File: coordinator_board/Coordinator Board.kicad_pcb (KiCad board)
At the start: 2 copper layers, 42.5 x 27 mm, 19 parts, among them P1 POWER, P4 SERIAL, SW1 Switch_SPDT_x2, SW2 Switch_DPST, U1 LM3671, U3 ESP-12E, U4 DIY-OLED-0.96, U5 SF303GJ26

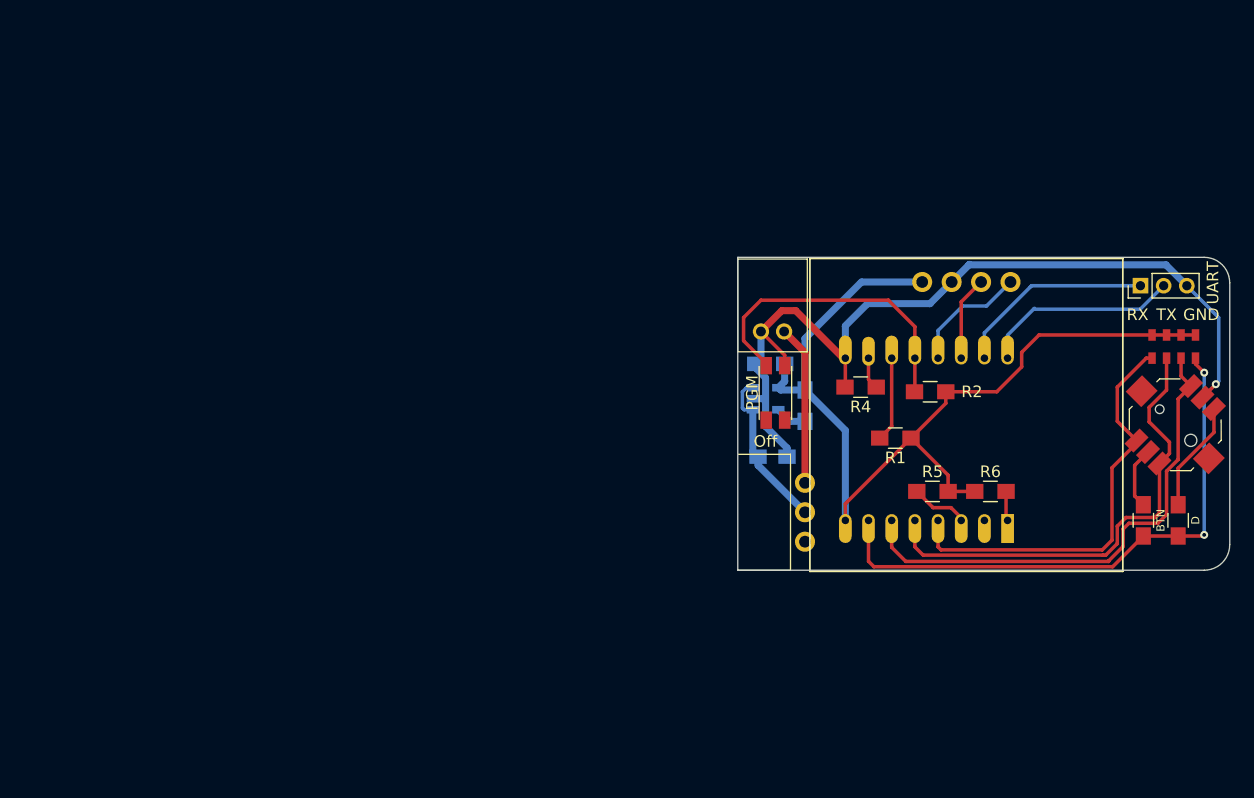
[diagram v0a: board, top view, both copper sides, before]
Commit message: Created new part layout
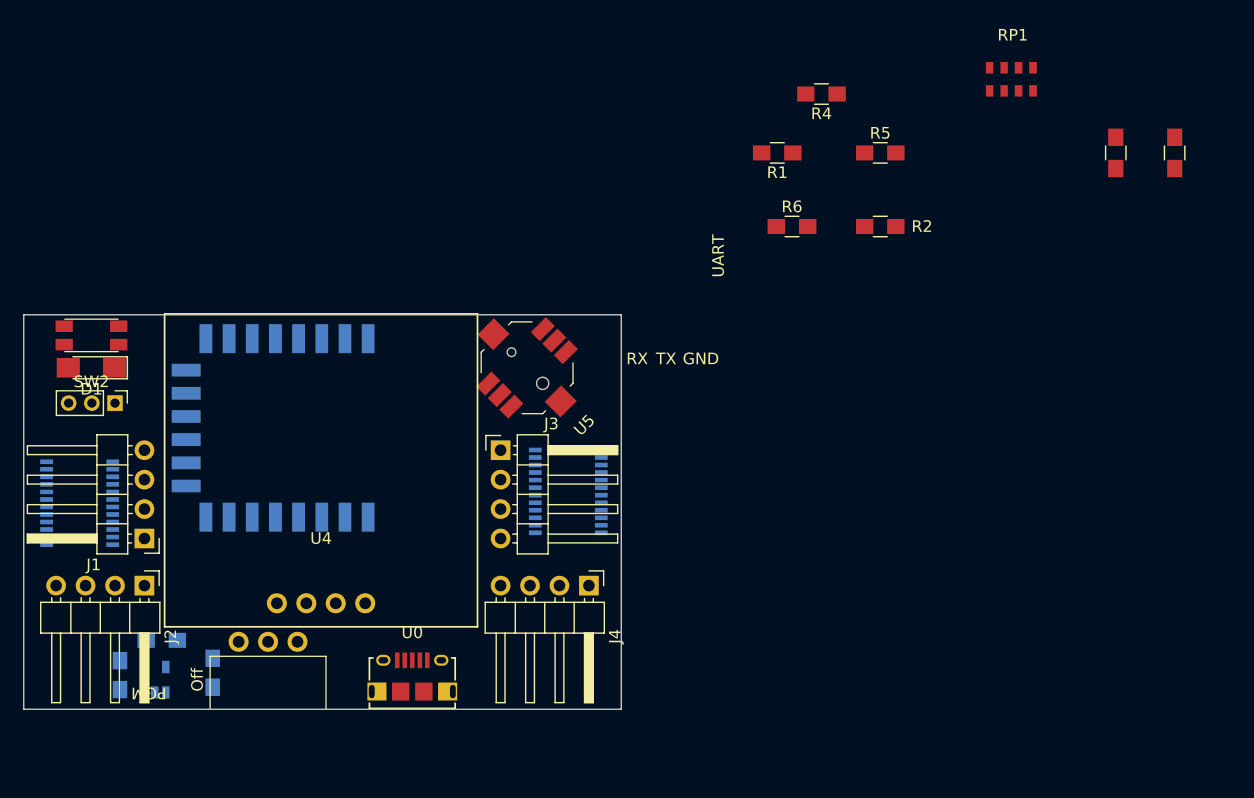
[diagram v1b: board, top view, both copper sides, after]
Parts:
- removed P1: POWER, PH_Connector:S2B-PH-K-S
- added D1: LED, LEDs:LED_1206_HandSoldering, F.Cu at (94.4, 107.7)
- added J1: Conn_01x04, Pin_Headers:Pin_Header_Angled_1x04_Pitch2.54mm, F.Cu at (99.0, 122.5)
- added J2: Conn_01x04, Pin_Headers:Pin_Header_Angled_1x04_Pitch2.54mm, F.Cu at (99.0, 126.5)
- added J3: Conn_01x04, Pin_Headers:Pin_Header_Angled_1x04_Pitch2.54mm, F.Cu at (129.7, 114.8)
- added J4: Conn_01x04, Pin_Headers:Pin_Header_Angled_1x04_Pitch2.54mm, F.Cu at (137.4, 126.5)
- added U0: 10118194, nebrius-conn:10118194, F.Cu at (122.1, 135.7)
- added U6: CD40109B, Housings_SSOP:TSSOP-24_4.4x7.8mm_Pitch0.65mm, B.Cu at (93.4, 119.4)
- added U7: CD40109B, Housings_SSOP:TSSOP-24_4.4x7.8mm_Pitch0.65mm, B.Cu at (135.6, 118.4)
- R7: value 0 -> 10k
- RP1: footprint R_Array:R_Array_Concave_4x0805 -> nebrius-discrete:R_Array_Concave_4x0805
- SW2: footprint KMR6:KMR641NG -> nebrius-switch:KMR641NG
- U3: footprint ESP8266:ESP-12 -> ESP8266:ESP-12E_SMD
- U4: footprint DIY-OLED:DIY-OLED-0.96 -> nebrius-lcd:DIY-OLED-0.96
- U5: footprint SF303GJ26:SF303GJ26 -> nebrius-switch:SF303GJ26
- moved P4 89.1 mm to (96.5, 110.8), turned to 270 degrees
- moved U4 64.1 mm to (114.2, 130.1), turned to 180 degrees
- moved C2 62.2 mm to (96.9, 134.2), turned to 270 degrees
- moved SW2 59.2 mm to (94.4, 104.9), turned to 0 degrees
- moved L1 59.1 mm to (100.5, 131.2), turned to 180 degrees
- moved U1 58.0 mm to (99.9, 134.7), turned to 90 degrees
- moved U5 56.1 mm to (132.0, 107.7)
- moved U3 55.2 mm to (118.3, 119.9)
- moved C1 51.8 mm to (104.9, 134.1), turned to 90 degrees
- moved SW1 47.7 mm to (109.7, 131.4), turned to 0 degrees
- moved R7 32.2 mm to (182.8, 89.2)
- moved R8 31.8 mm to (187.9, 89.2)
- moved R5 29.6 mm to (162.5, 89.2)
- moved R6 28.6 mm to (154.9, 95.5)
- moved RP1 27.0 mm to (173.9, 82.8)
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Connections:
- net Net-(C1-Pad1) renamed +5V
- R7 pad 1: Net-(R7-Pad1) -> +3V3
- R8 pad 1: Net-(R7-Pad1) -> Net-(D1-Pad1)
- R8 pad 2: Net-(R8-Pad2) -> GND
- RP1 pad 4: Net-(R7-Pad1) -> Net-(RP1-Pad4)
- U3 pad 7: Net-(R7-Pad1) -> Net-(RP1-Pad4)
- U5 pad 2: Net-(R8-Pad2) -> Net-(R7-Pad2)
- U5 pad 6: Net-(R7-Pad2) -> Net-(RP1-Pad4)
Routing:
- net +3V3: track 81.6 -> 0.00 mm
- net GND: track 76.2 -> 0.00 mm, vias 1 -> 0
- net Net-(R7-Pad1): track 49.4 -> 0.00 mm, vias 2 -> 0
- net Net-(RP1-Pad3): track 43.9 -> 0.00 mm
- net Net-(RP1-Pad2): track 41.1 -> 0.00 mm
- net Net-(RP1-Pad1): track 36.5 -> 0.00 mm
- net Net-(R2-Pad1): track 27.9 -> 0.00 mm
- net Net-(P4-Pad1): track 19.1 -> 0.00 mm
- net Net-(P4-Pad2): track 18.7 -> 0.00 mm
- net +5V: track 14.1 -> 0.00 mm
- net Net-(SW1-Pad1): track 13.8 -> 0.00 mm
- net Net-(U3-Pad13): track 10.4 -> 0.00 mm
- net Net-(R7-Pad2): track 9.54 -> 0.00 mm
- net Net-(R1-Pad2): track 7.32 -> 0.00 mm
- net Net-(U3-Pad14): track 7.28 -> 0.00 mm
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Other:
- board size 42.5 x 27 mm -> 51.6 x 34 mm
- board text removed: "BTN"
- board text removed: "D"

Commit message: Finished most of the layout
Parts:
- R5, R6: moved to B.Cu
- moved R8 99.9 mm to (90.0, 109.1), turned to 270 degrees
- moved R7 81.8 mm to (105.6, 116.1), turned to 270 degrees
- moved RP1 72.1 mm to (109.9, 116.1)
- moved R4 61.7 mm to (99.5, 105.4)
- moved R5 58.6 mm to (116.8, 125.8)
- moved R2 56.7 mm to (108.4, 112.6), turned to 180 degrees
- moved R1 49.9 mm to (108.4, 110.3), turned to 0 degrees
- moved R6 44.4 mm to (122.4, 125.8)
- moved U1 6.03 mm to (103.8, 130.1)
- moved L1 5.70 mm to (104.3, 127.0)
- moved C2 5.70 mm to (100.8, 130.1)
- moved C1 2.62 mm to (102.3, 133.6), turned to 180 degrees
- moved P4 2.09 mm to (98.5, 111.3)
- moved U5 2.09 mm to (134.1, 108.2)
- moved SW2 2.03 mm to (92.4, 104.9)
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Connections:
- SW1 pad 1: Net-(SW1-Pad1) -> (no net)
- SW1 pad 3: (no net) -> Net-(SW1-Pad3)
- U0 pad 1: Net-(SW1-Pad1) -> Net-(SW1-Pad3)
- U3 pad 13: Net-(U3-Pad13) -> Net-(RP1-Pad4)
- U3 pad 14: Net-(U3-Pad14) -> Net-(RP1-Pad3)
- U3 pad 4: Net-(RP1-Pad1) -> Net-(U3-Pad4)
- U3 pad 5: Net-(RP1-Pad2) -> Net-(U3-Pad5)
- U3 pad 6: Net-(RP1-Pad3) -> Net-(RP1-Pad2)
- U3 pad 7: Net-(RP1-Pad4) -> Net-(RP1-Pad1)
- U4 pad 3: Net-(U3-Pad14) -> Net-(U3-Pad4)
- U4 pad 4: Net-(U3-Pad13) -> Net-(U3-Pad5)
- U5 pad 1: Net-(RP1-Pad1) -> Net-(R7-Pad2)
- U5 pad 2: Net-(R7-Pad2) -> Net-(RP1-Pad2)
- U5 pad 3: Net-(RP1-Pad2) -> Net-(RP1-Pad1)
- U5 pad 4: Net-(RP1-Pad3) -> Net-(RP1-Pad4)
- U5 pad 6: Net-(RP1-Pad4) -> Net-(RP1-Pad3)
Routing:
- net Net-(RP1-Pad1): track 0.00 -> 49.5 mm, vias 0 -> 1
- net Net-(RP1-Pad2): track 0.00 -> 45.3 mm, vias 0 -> 1
- net Net-(R7-Pad2): track 0.00 -> 45.2 mm, vias 0 -> 2
- net Net-(RP1-Pad3): track 0.00 -> 42.9 mm, vias 0 -> 2
- net Net-(RP1-Pad4): track 0.00 -> 37.9 mm, vias 0 -> 2
- net Net-(P4-Pad2): track 0.00 -> 28.7 mm
- net Net-(R2-Pad1): track 0.00 -> 24.8 mm, vias 0 -> 2
- net Net-(P4-Pad1): track 0.00 -> 24.5 mm
- net GND: track 0.00 -> 21.7 mm, vias 0 -> 5
- net +3V3: track 0.00 -> 21.4 mm, vias 0 -> 4
- net Net-(D1-Pad2): track 0.00 -> 10.4 mm, vias 0 -> 1
- net Net-(SW1-Pad3): track 0.00 -> 9.61 mm
- net Net-(R6-Pad2): track 0.00 -> 8.84 mm
- net Net-(R4-Pad1): track 0.00 -> 8.61 mm, vias 0 -> 1
- net Net-(U3-Pad4): track 0.00 -> 6.88 mm
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- added copper zone on Power.Plane, net +3V3
- added copper zone on Power.Plane, net +5V
- added copper zone on Ground.Plane, net GND
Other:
- copper layers 2 -> 4
- board text removed: "RX"
- board text removed: "TX"
- board text removed: "UART"

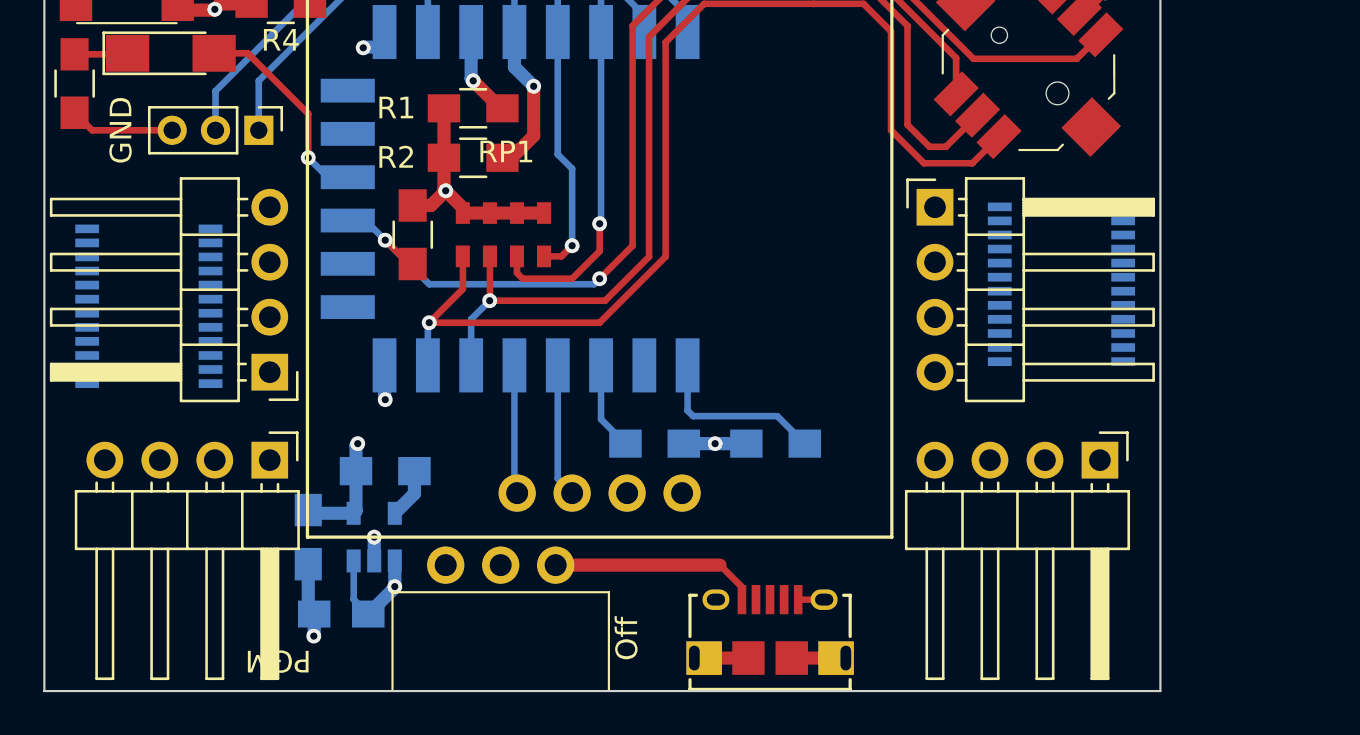
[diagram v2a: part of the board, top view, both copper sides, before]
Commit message: Revised schematic and added BOM
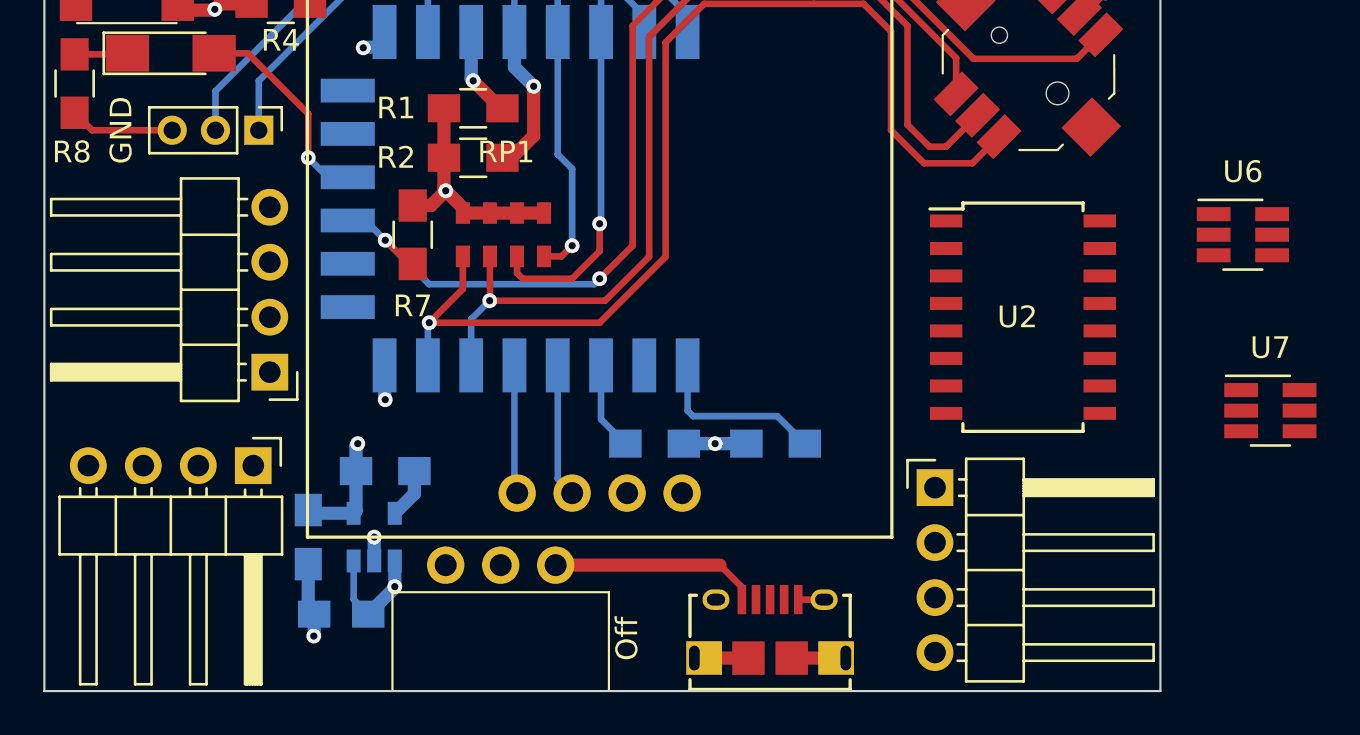
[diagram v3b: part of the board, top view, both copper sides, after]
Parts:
- removed J4: Conn_01x04, Pin_Headers:Pin_Header_Angled_1x04_Pitch2.54mm
- added U2: CD74HC4050, Housings_SOIC:SOIC-16W_5.3x10.2mm_Pitch1.27mm, F.Cu at (133.8, 119.9)
- U6, U7: value CD40109B -> SN74LVC1T45; footprint Housings_SSOP:TSSOP-24_4.4x7.8mm_Pitch0.65mm -> TO_SOT_Packages_SMD:SOT-23-6_Handsoldering; moved to F.Cu
- moved U6 50.7 mm to (144.0, 116.1), turned to 0 degrees
- moved J3 13.0 mm to (129.7, 127.8)
- moved U7 11.3 mm to (145.2, 124.2)
- moved J2 0.80 mm to (98.2, 126.8)
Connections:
- U6 pad 1: +3V3 -> +5V
- U6 pad 2: +3V3 -> GND
- U6 pad 3: Net-(U3-Pad22) -> Net-(U2-Pad11)
- U6 pad 4: Net-(J1-Pad2) -> Net-(U3-Pad21)
- U6 pad 5: Net-(J2-Pad2) -> GND
- U6 pad 6: Net-(U3-Pad22) -> +5V
- U7 pad 1: +3V3 -> +5V
- U7 pad 2: +3V3 -> GND
- U7 pad 3: Net-(U3-Pad22) -> Net-(U2-Pad3)
- U7 pad 4: Net-(J3-Pad2) -> Net-(U3-Pad22)
- U7 pad 5: Net-(J4-Pad2) -> GND
- U7 pad 6: Net-(U3-Pad22) -> +5V
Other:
- board text added: "Raver Lights Coordinator v3.0 Copyright Bryan Hughes 2018"
- board text removed: "PGM"
- board text removed: "Raver Lights Coordinator v2.7 Copyright Bryan Hughes 2017"

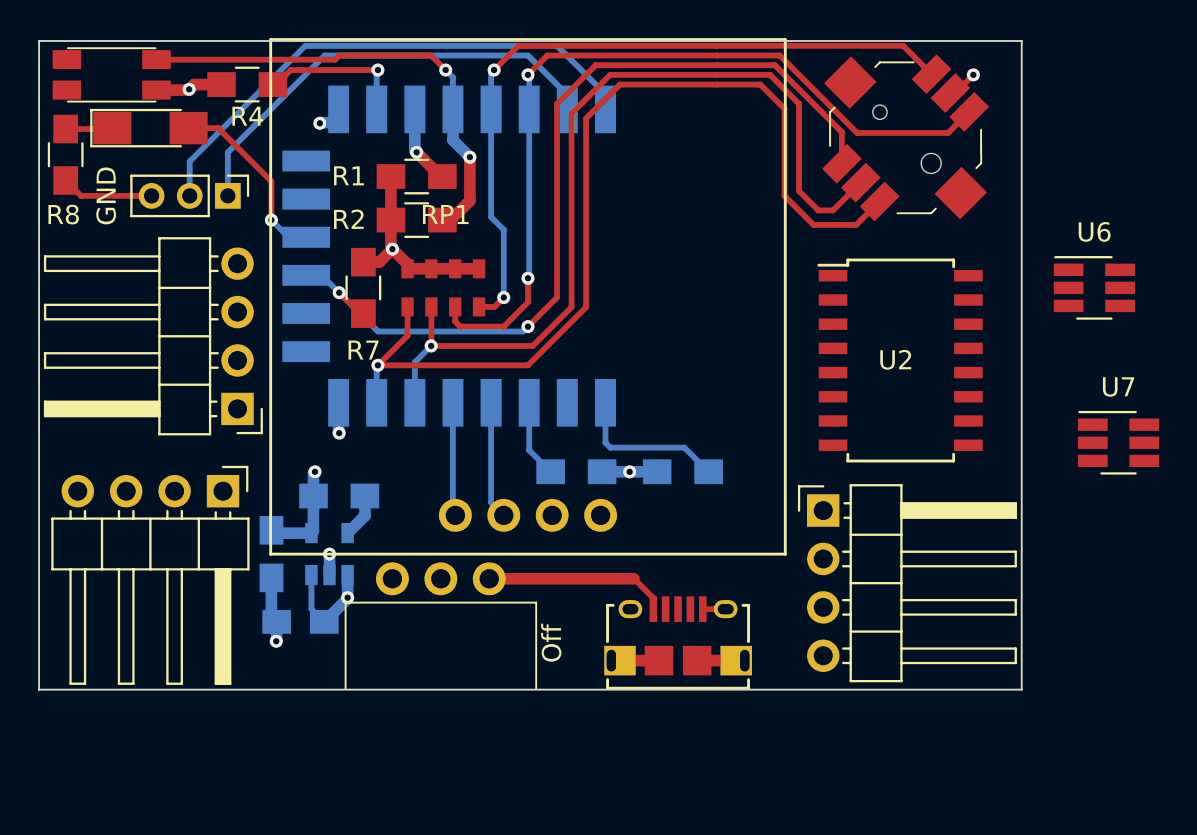
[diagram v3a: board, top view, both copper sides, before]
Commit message: Relaid out parts on board
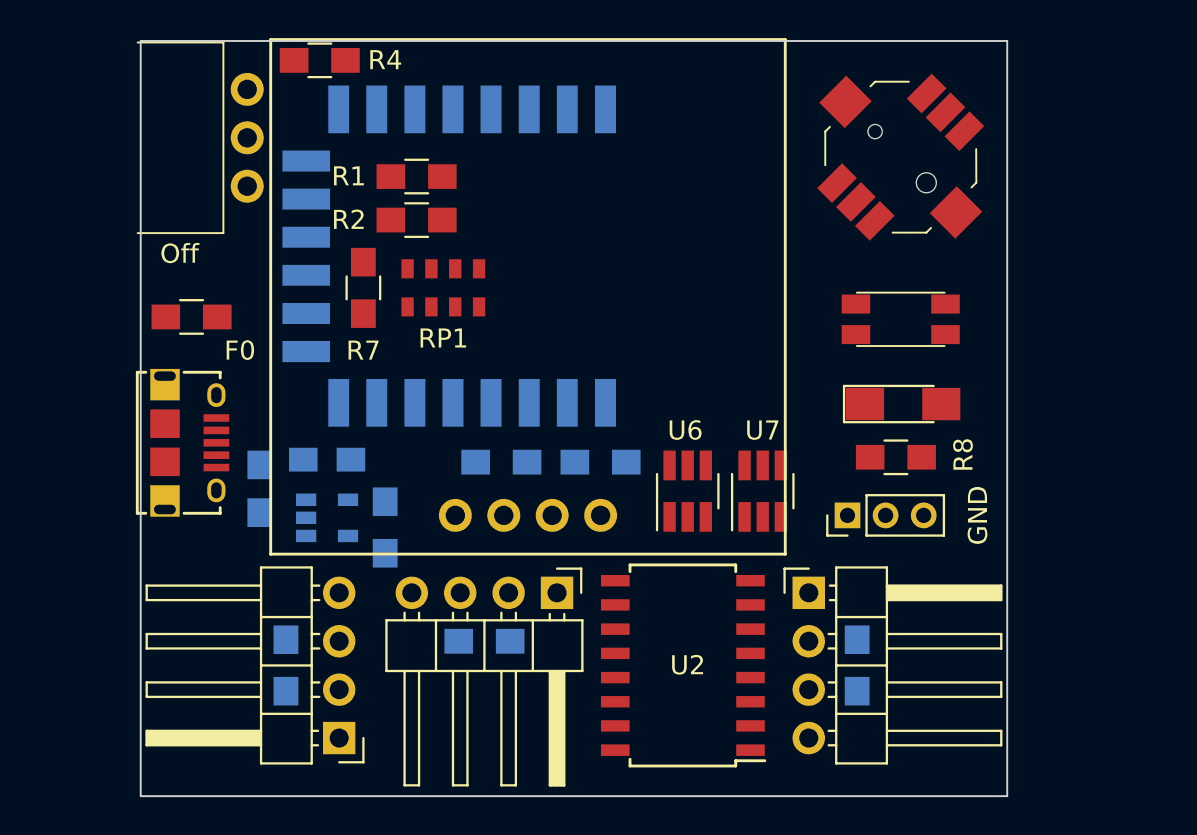
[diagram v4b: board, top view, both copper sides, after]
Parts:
- added C4: 10uF, Resistors_SMD:R_0805_HandSoldering, B.Cu at (112.0, 134.7)
- added C5: 10uF, Resistors_SMD:R_0805_HandSoldering, B.Cu at (101.5, 135.9)
- added C6: 10uF, Resistors_SMD:R_0805_HandSoldering, B.Cu at (131.5, 135.9)
- added F0: Fuse, Resistors_SMD:R_0805_HandSoldering, F.Cu at (96.6, 117.6)
- moved R8 46.4 mm to (133.5, 125.0), turned to 0 degrees
- moved SW2 43.3 mm to (133.8, 117.8), turned to 180 degrees
- moved D1 42.1 mm to (133.9, 122.2)
- moved P4 36.6 mm to (131.0, 128.1), turned to 90 degrees
- moved U0 29.2 mm to (95.2, 124.2), turned to 270 degrees
- moved SW1 25.3 mm to (99.5, 108.2), turned to 270 degrees
- moved U6 23.9 mm to (122.6, 126.8), turned to 90 degrees
- moved U2 19.7 mm to (122.4, 135.9), turned to 180 degrees
- moved U7 18.8 mm to (126.6, 126.8), turned to 90 degrees
- moved J2 18.3 mm to (115.8, 132.1)
- moved J1 18.1 mm to (104.3, 139.7)
- moved C1 7.31 mm to (100.1, 126.7), turned to 90 degrees
- moved C2 5.75 mm to (103.7, 125.1), turned to 180 degrees
- moved J3 4.38 mm to (129.0, 132.1)
- moved R6 4.35 mm to (118.0, 125.3)
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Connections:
- SW1 pad 3: Net-(SW1-Pad3) -> Net-(F0-Pad1)
- U0 pad 1: Net-(SW1-Pad3) -> Net-(F0-Pad2)
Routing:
- net Net-(RP1-Pad1): track 49.5 -> 0.00 mm, vias 1 -> 0
- net Net-(RP1-Pad2): track 45.3 -> 0.00 mm, vias 1 -> 0
- net Net-(R7-Pad2): track 45.2 -> 0.00 mm, vias 2 -> 0
- net Net-(RP1-Pad3): track 42.9 -> 0.00 mm, vias 2 -> 0
- net Net-(RP1-Pad4): track 37.9 -> 0.00 mm, vias 2 -> 0
- net Net-(P4-Pad2): track 28.7 -> 0.00 mm
- net Net-(R2-Pad1): track 24.8 -> 0.00 mm, vias 2 -> 0
- net Net-(P4-Pad1): track 24.5 -> 0.00 mm
- net GND: track 21.7 -> 0.00 mm, vias 5 -> 0
- net +3V3: track 21.4 -> 0.00 mm, vias 4 -> 0
- net Net-(D1-Pad2): track 10.4 -> 0.00 mm, vias 1 -> 0
- net Net-(SW1-Pad3): track 9.61 -> 0.00 mm
- net Net-(R6-Pad2): track 8.84 -> 0.00 mm
- net Net-(R4-Pad1): track 8.61 -> 0.00 mm, vias 1 -> 0
- net Net-(U3-Pad4): track 6.88 -> 0.00 mm
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- removed copper zone on Power.Plane, net +3V3
- removed copper zone on Power.Plane, net +5V
- removed copper zone on Ground.Plane, net GND
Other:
- board size 51.6 x 34 mm -> 45.5 x 39.6 mm
